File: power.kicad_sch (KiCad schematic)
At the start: 0 parts

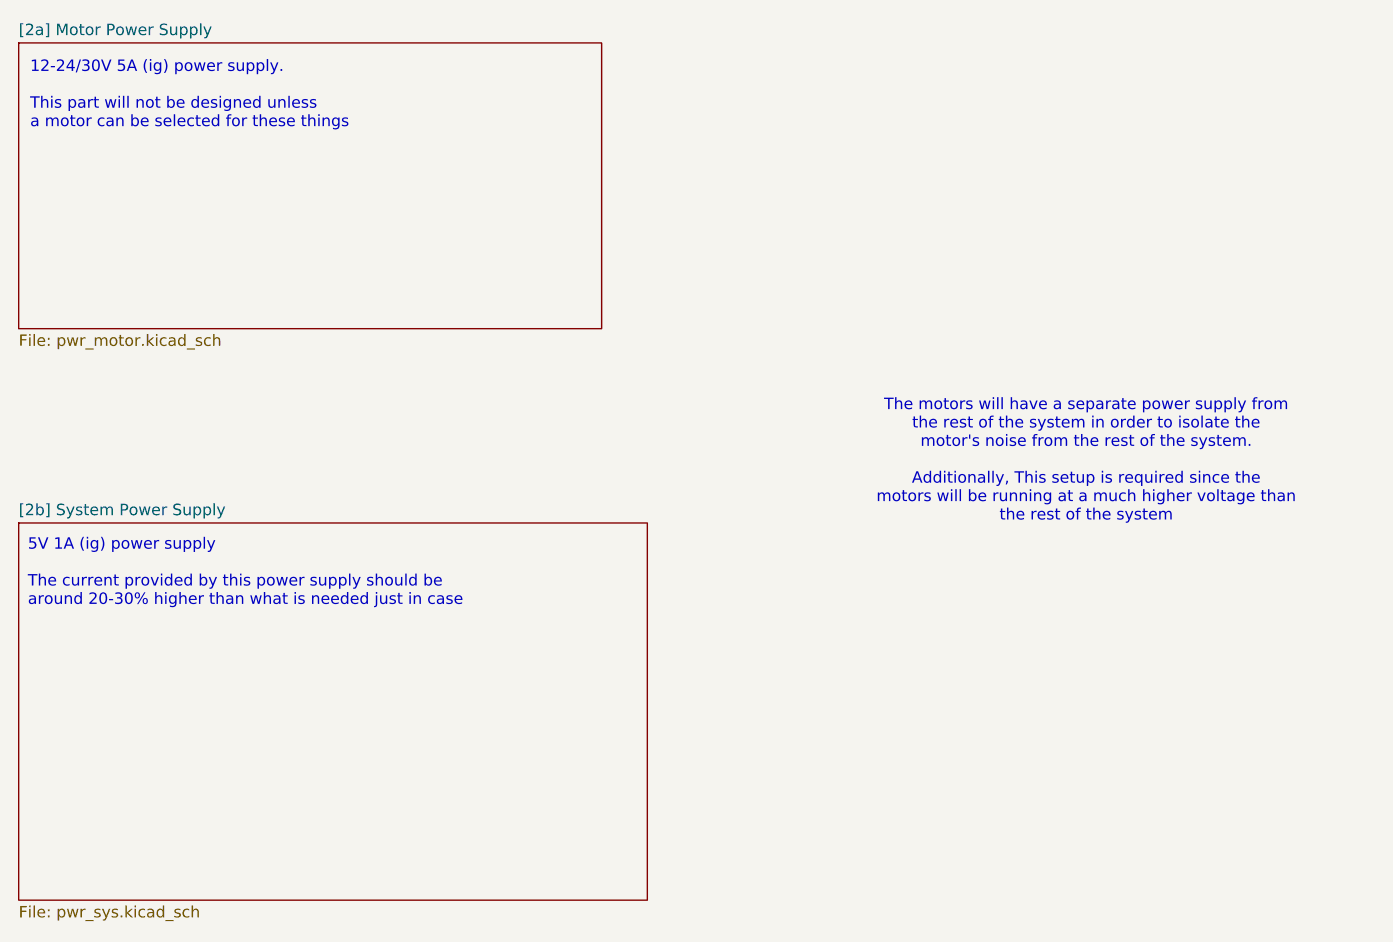
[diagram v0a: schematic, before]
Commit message: chore(pcb): finalized current requirements
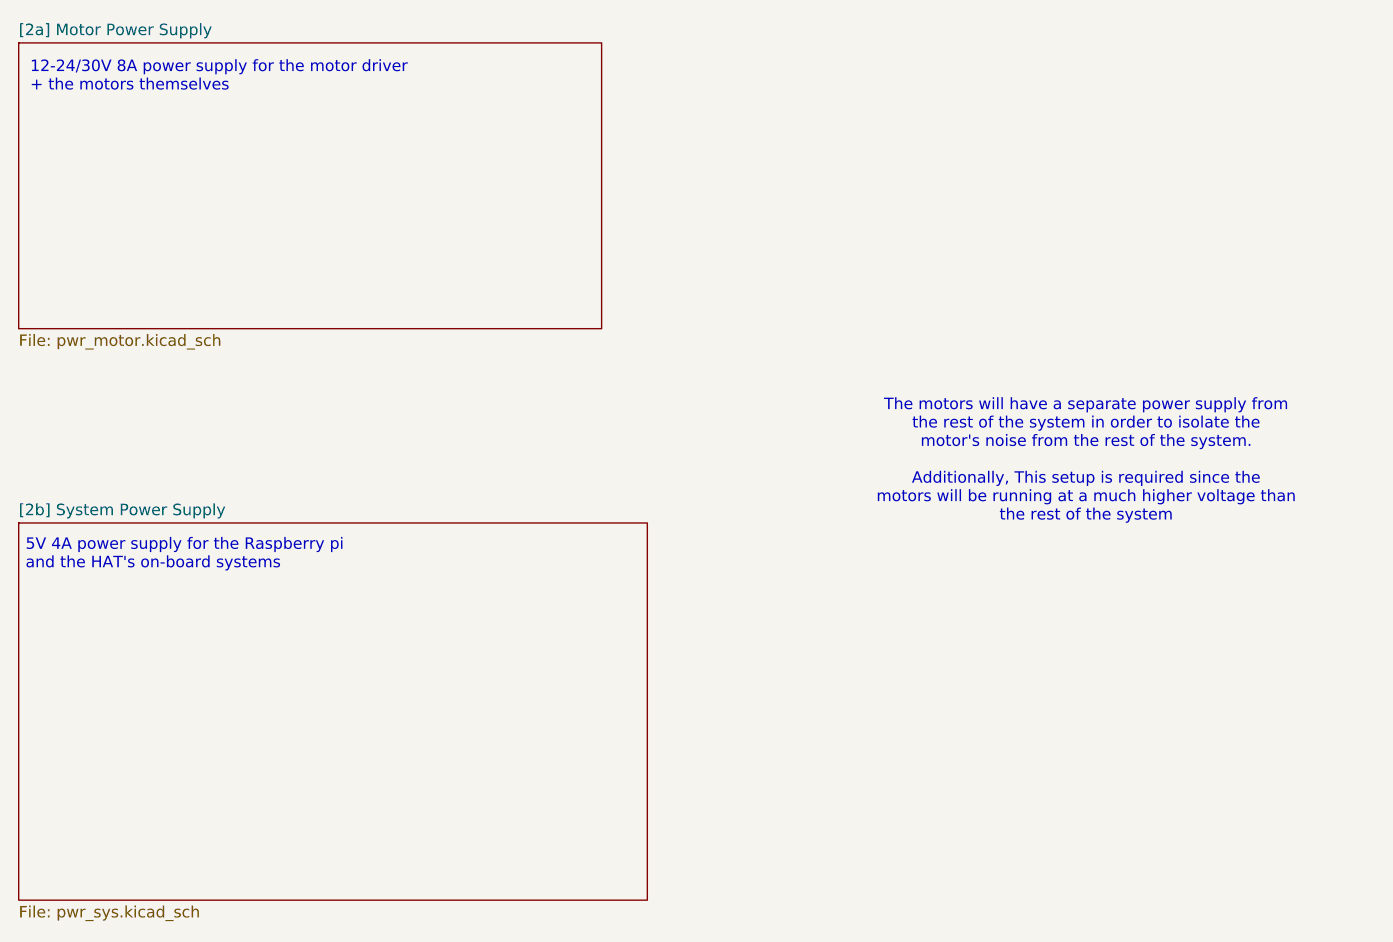
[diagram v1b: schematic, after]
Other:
- note added: "12-24/30V 8A power supply for the motor driver + the motors themselves"
- note added: "5V 4A power supply for the Raspberry pi and the HAT's on-board systems"
- note removed: "12-24/30V 5A (ig) power supply. This part will not be designed unless a motor can be selected for these things"
- note removed: "5V 1A (ig) power supply The current provided by this power supply should be around 20-30% higher than what is needed just in case"
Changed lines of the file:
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@@
 		(company "Mixed Engineering Group 3 | STEM 12-Altruism / AY 2526 | CIT-U SHS")
 	)
-	(text "12-24/30V 5A (ig) power supply.\n\nThis part will not be designed unless\na motor can be selected for these things"
+	(text "12-24/30V 8A power supply for the motor driver\n+ the motors themselves"
 		(exclude_from_sim no)
-		(at 58.42 37.592 0)
+		(at 58.42 35.56 0)
 		(effects
 			(font
@@
 		)
 	)
-	(text "5V 1A (ig) power supply\n\nThe current provided by this power supply should be\naround 20-30% higher than what is needed just in case"
+	(text "5V 4A power supply for the Raspberry pi\nand the HAT's on-board systems"
 		(exclude_from_sim no)
-		(at 58.166 90.678 0)
+		(at 57.912 88.646 0)
 		(effects
 			(font

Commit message: feat: nets and stuff?? I guess?
I don't really remember what this commit changes
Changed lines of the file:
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@@
 	(text "The motors will have a separate power supply from\nthe rest of the system in order to isolate the\nmotor's noise from the rest of the system.\n\nAdditionally, This setup is required since the\nmotors will be running at a much higher voltage than\nthe rest of the system"
 		(exclude_from_sim no)
-		(at 175.768 78.232 0)
+		(at 169.926 49.784 0)
 		(effects
 			(font
